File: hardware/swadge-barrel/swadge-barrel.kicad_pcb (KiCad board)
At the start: 2 copper layers, 70.4 x 89.6 mm, 47 parts, among them J1 USB_B_Micro, Q1 Q_NPN_BEC, SW1 SW_SPDT, U1 ESP-13-WROOM-02D, U2 OLED_DISPLAY, U3 BUS_PCIexpress, U4 QMA6981, U5 AP1117-33, U6 OLED_CONNECTOR

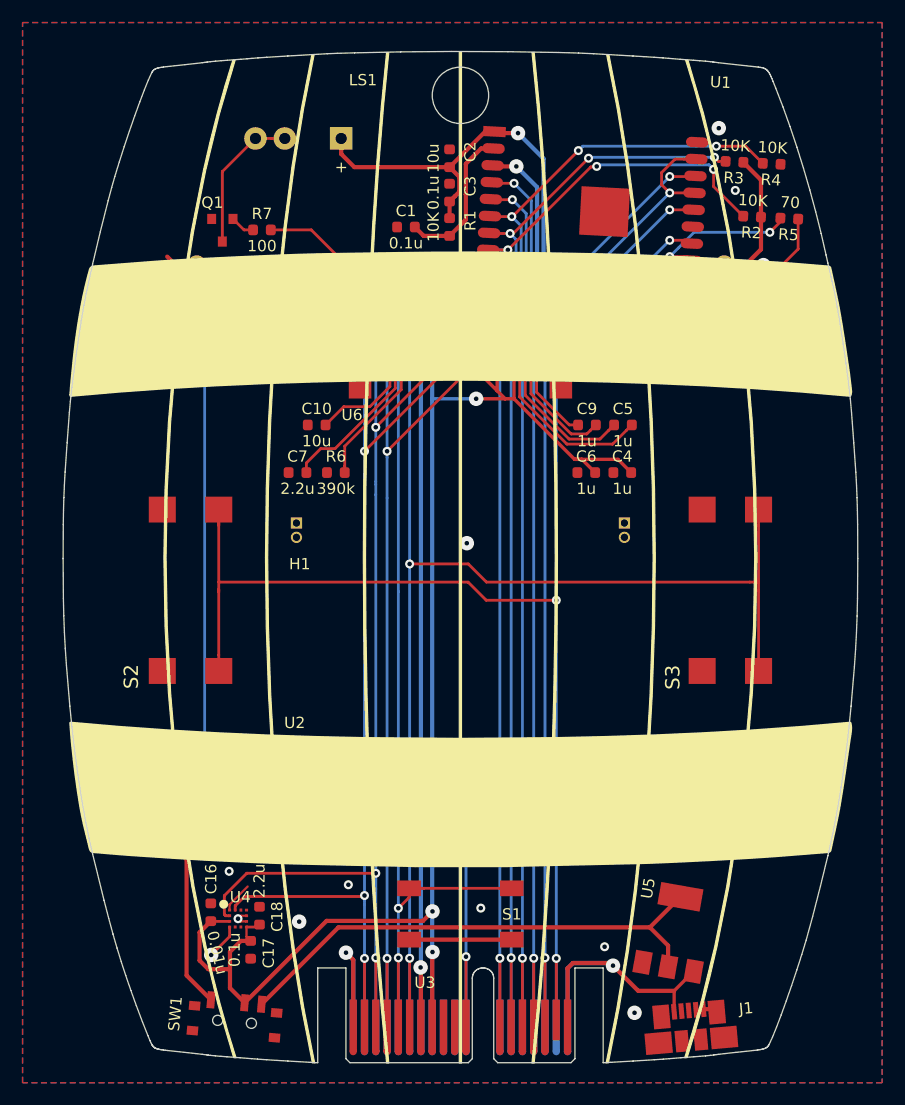
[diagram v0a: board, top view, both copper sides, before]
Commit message: Removed transistor from the buzzer circuit. It's louder this way Updated buzzer part info Updated headband part info Adjusted orientation of accelerometer passives
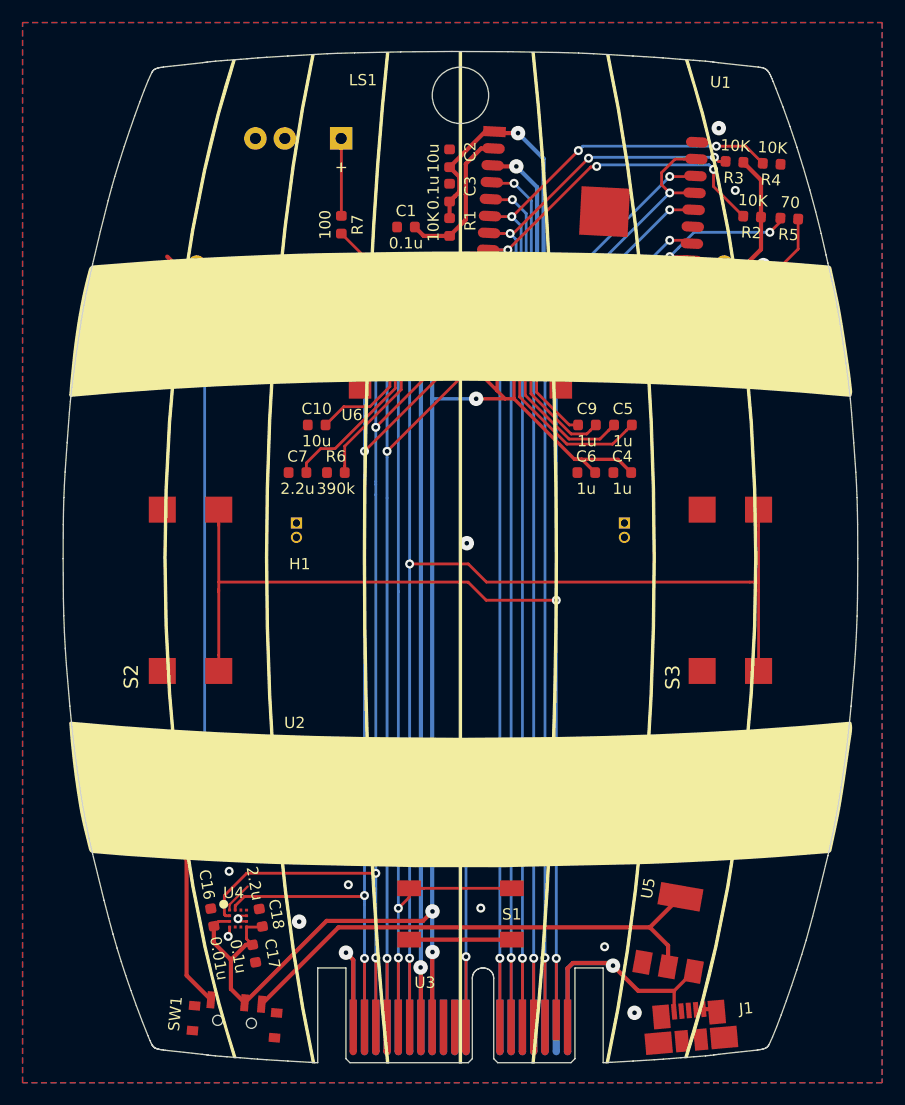
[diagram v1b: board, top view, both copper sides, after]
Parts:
- removed Q1: Q_NPN_BEC, Swadge_Parts:SOT-23
- moved R7 7.06 mm to (134.9, 68.7), turned to 270 degrees
- moved C16 0.47 mm to (123.5, 130.1), turned to 100 degrees
- moved C17 0.45 mm to (127.2, 133.3), turned to 280 degrees
- moved C18 0.21 mm to (127.8, 130.2), turned to 100 degrees
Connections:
- LS1 pad 1: +3V3 -> Net-(LS1-Pad1)
- LS1 pad 2: Net-(LS1-Pad2) -> GND
- R7 pad 1: Net-(Q1-Pad1) -> Net-(LS1-Pad1)
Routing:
- net +3V3: track 310.1 -> 295.5 mm
- net Net-(LS1-Pad2): track 13.4 -> 0.00 mm
- net Net-(LS1-Pad1): track 0.00 -> 6.86 mm
- net BZR: track 116.9 -> 110.5 mm
- net Net-(Q1-Pad1): track 2.17 -> 0.00 mm
- net GND: track 73.3 -> 71.4 mm

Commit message: Removed some capacitance from 3.3V, added some capacitance to 5V
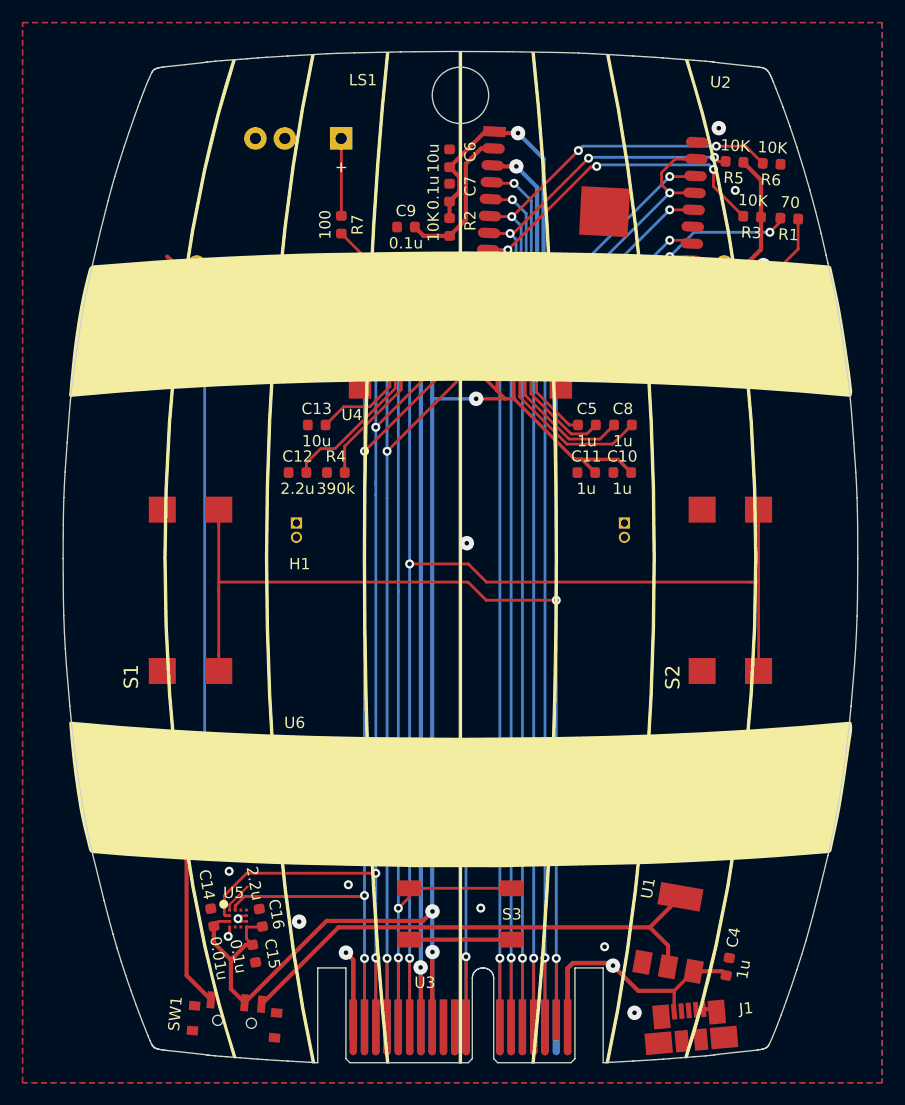
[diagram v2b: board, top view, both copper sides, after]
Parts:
- removed the C13 at (169.7, 122.3)
- removed the C15 at (121.3, 122.3)
- moved C4 64.9 mm to (169.2, 134.5), turned to 80 degrees
- renumbered C8 to C1, C4 to C10, C6 to C11, C7 to C12, C10 to C13, C16 to C14, C17 to C15, C18 to C16, C12 to C2, C14 to C3, C11 to C4, C9 to C5, C2 to C6, C3 to C7, C5 to C8, C1 to C9, R5 to R1, R1 to R2, R2 to R3, R6 to R4, R3 to R5, R4 to R6, S2 to S1, S3 to S2, S1 to S3, U5 to U1, U1 to U2, U6 to U4, U4 to U5, U2 to U6
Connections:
- C4 pad 1: +3V3 -> +5V
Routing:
- net +3V3: track 295.5 -> 288.6 mm
- net +5V: track 29.4 -> 32.5 mm
- net GND: track 71.4 -> 69.6 mm

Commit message: Incremetned barrel version
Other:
- board text added: "Barrel 1.0.2"
- board text removed: "Barrel 1.0.1"
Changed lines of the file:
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@@
   (gr_poly (pts (xy 139.146221 53.453374) (xy 138.944683 53.457508) (xy 138.476254 58.27004) (xy 138.064585 63.372615) (xy 137.711432 68.732148) (xy 137.418549 74.31556) (xy 137.187695 80.089768) (xy 137.020624 86.021689) (xy 136.919094 92.078243) (xy 136.884861 98.226347) (xy 136.919177 104.381366) (xy 137.02095 110.444519) (xy 137.188414 116.382634) (xy 137.419805 122.162535) (xy 137.713358 127.751049) (xy 138.067307 133.115002) (xy 138.479887 138.22122) (xy 138.949335 143.036528) (xy 139.150356 143.036528) (xy 138.6808 138.223448) (xy 138.268071 133.118543) (xy 137.913953 127.755126) (xy 137.620225 122.166512) (xy 137.38867 116.386013) (xy 137.221067 110.446944) (xy 137.1192 104.382617) (xy 137.084848 98.226347) (xy 137.119126 92.076249) (xy 137.220778 86.017839) (xy 137.38803 80.084342) (xy 137.619108 74.308981) (xy 137.91224 68.72498) (xy 138.265652 63.365563) (xy 138.67757 58.263953) (xy 139.146221 53.453374)) (layer F.SilkS) (width 0.099999))
   (gr_poly (pts (xy 125.53 54.12) (xy 125.313993 54.136536) (xy 124.597446 56.483852) (xy 123.922624 58.903932) (xy 123.29015 61.392848) (xy 122.700644 63.946674) (xy 121.653024 69.23335) (xy 120.784734 74.732551) (xy 120.100745 80.412863) (xy 119.606027 86.242874) (xy 119.305551 92.191172) (xy 119.204288 98.226347) (xy 119.306883 104.300657) (xy 119.611286 110.286704) (xy 120.112422 116.152471) (xy 120.805217 121.865938) (xy 121.684597 127.395088) (xy 122.745488 132.707903) (xy 123.982816 137.772365) (xy 125.391507 142.556456) (xy 125.606998 142.572996) (xy 124.880258 140.220462) (xy 124.195694 137.793166) (xy 123.553957 135.295151) (xy 122.955696 132.730464) (xy 121.892203 127.417257) (xy 121.010414 121.885906) (xy 120.315527 116.168776) (xy 119.812743 110.29823) (xy 119.50726 104.306632) (xy 119.404276 98.226347) (xy 119.505949 92.185228) (xy 119.807562 86.231435) (xy 120.304009 80.396709) (xy 120.990182 74.712791) (xy 121.860975 69.21142) (xy 122.91128 63.924338) (xy 124.135991 58.883284) (xy 125.53 54.12)) (layer F.SilkS) (width 0.099999))
-  (gr_text "Barrel 1.0.1" (at 128.625 57.325) (layer B.SilkS)
+  (gr_text "Barrel 1.0.2" (at 128.625 57.325) (layer B.SilkS)
     (effects (font (size 2 2) (thickness 0.3)) (justify mirror))
   )
